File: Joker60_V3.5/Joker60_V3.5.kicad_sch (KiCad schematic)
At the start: 186 parts, among them J1 Conn_01x02, J2 Conn_01x04_MountingPin, J3 Conn_01x02, J4 Conn_01x02_MountingPin, J5 Conn_01x04_MountingPin, J6 Conn_01x06, U1 RP2040, U2 AMS1117-3.3, U3 W25Q128JVS, U4 2U卫星轴, U5 6.25u卫星轴, U6 2U卫星轴, U7 2U卫星轴, U8 2U卫星轴, U9 Oled_0.96_4P, Y1 Crystal

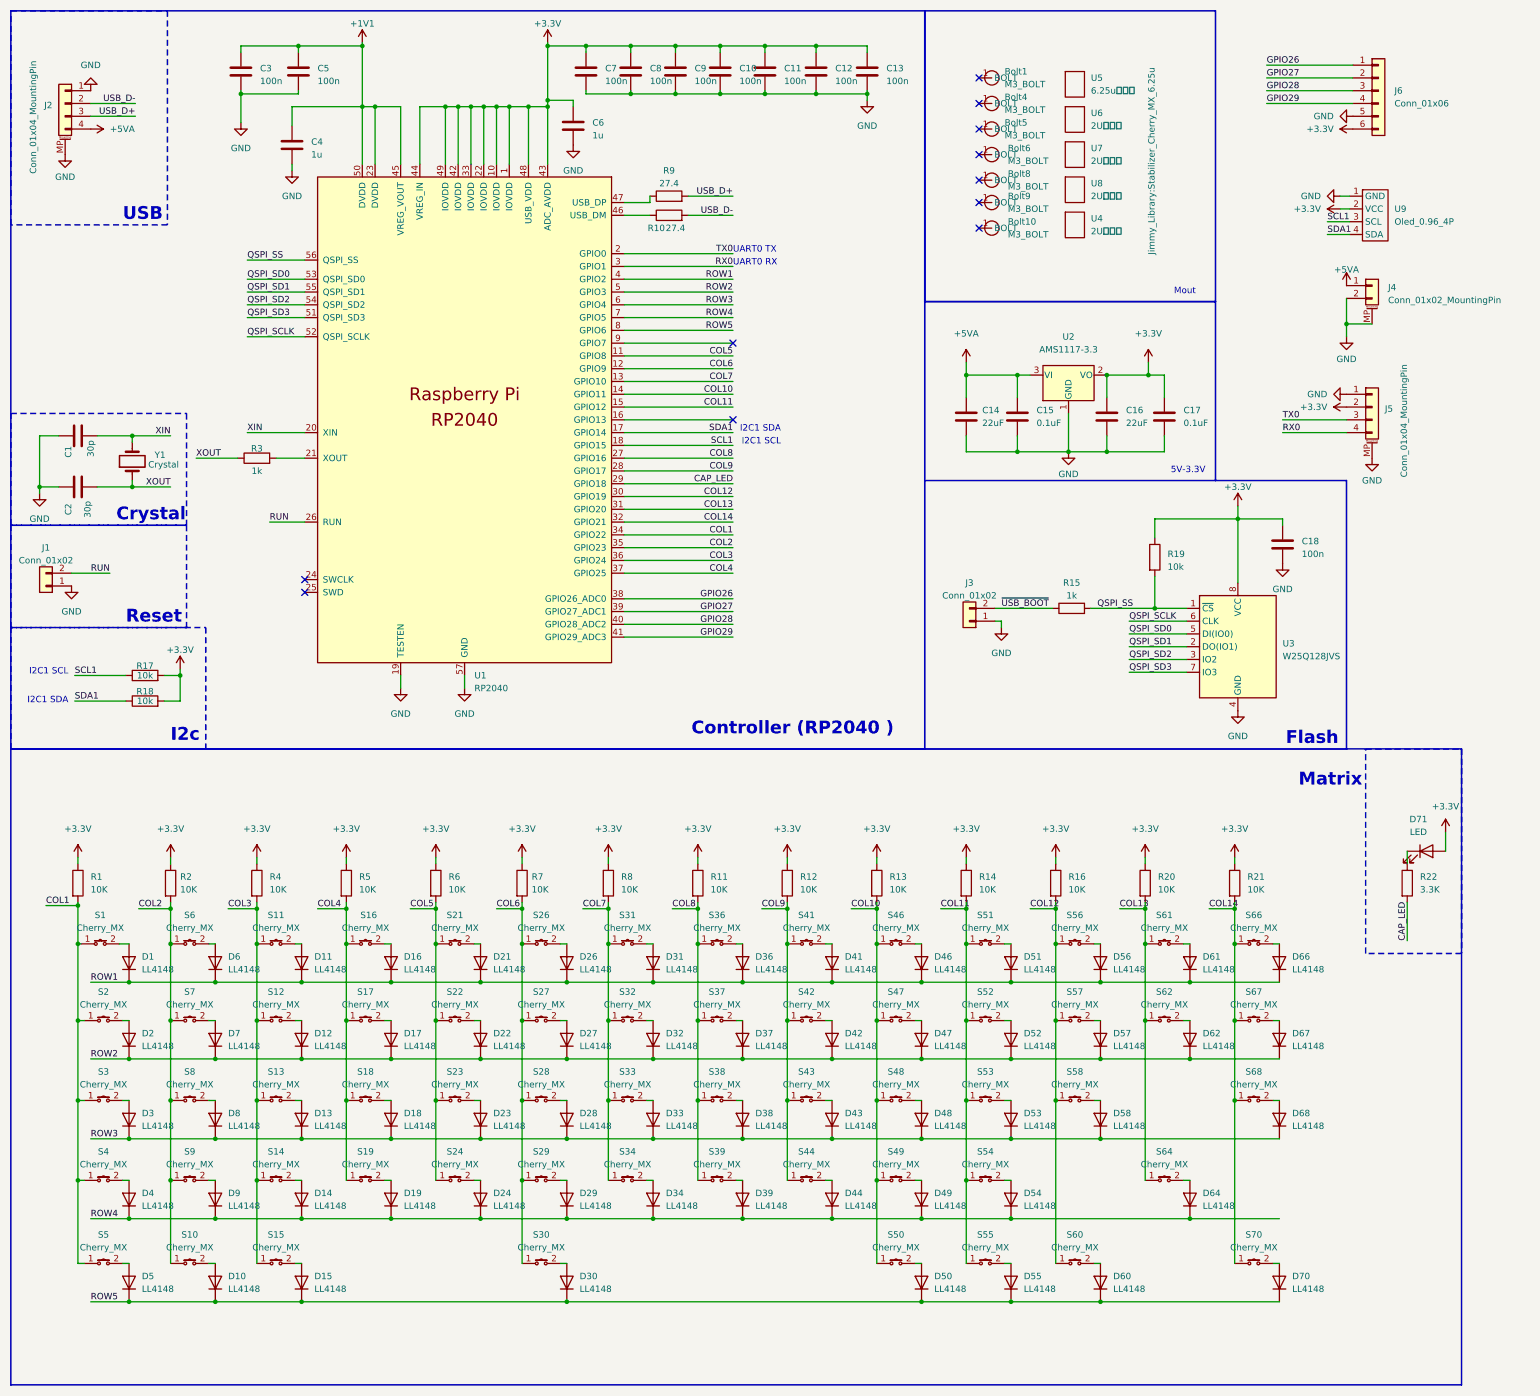
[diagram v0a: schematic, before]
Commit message: Start Building
Using Stm32f401, f103 should be compatible
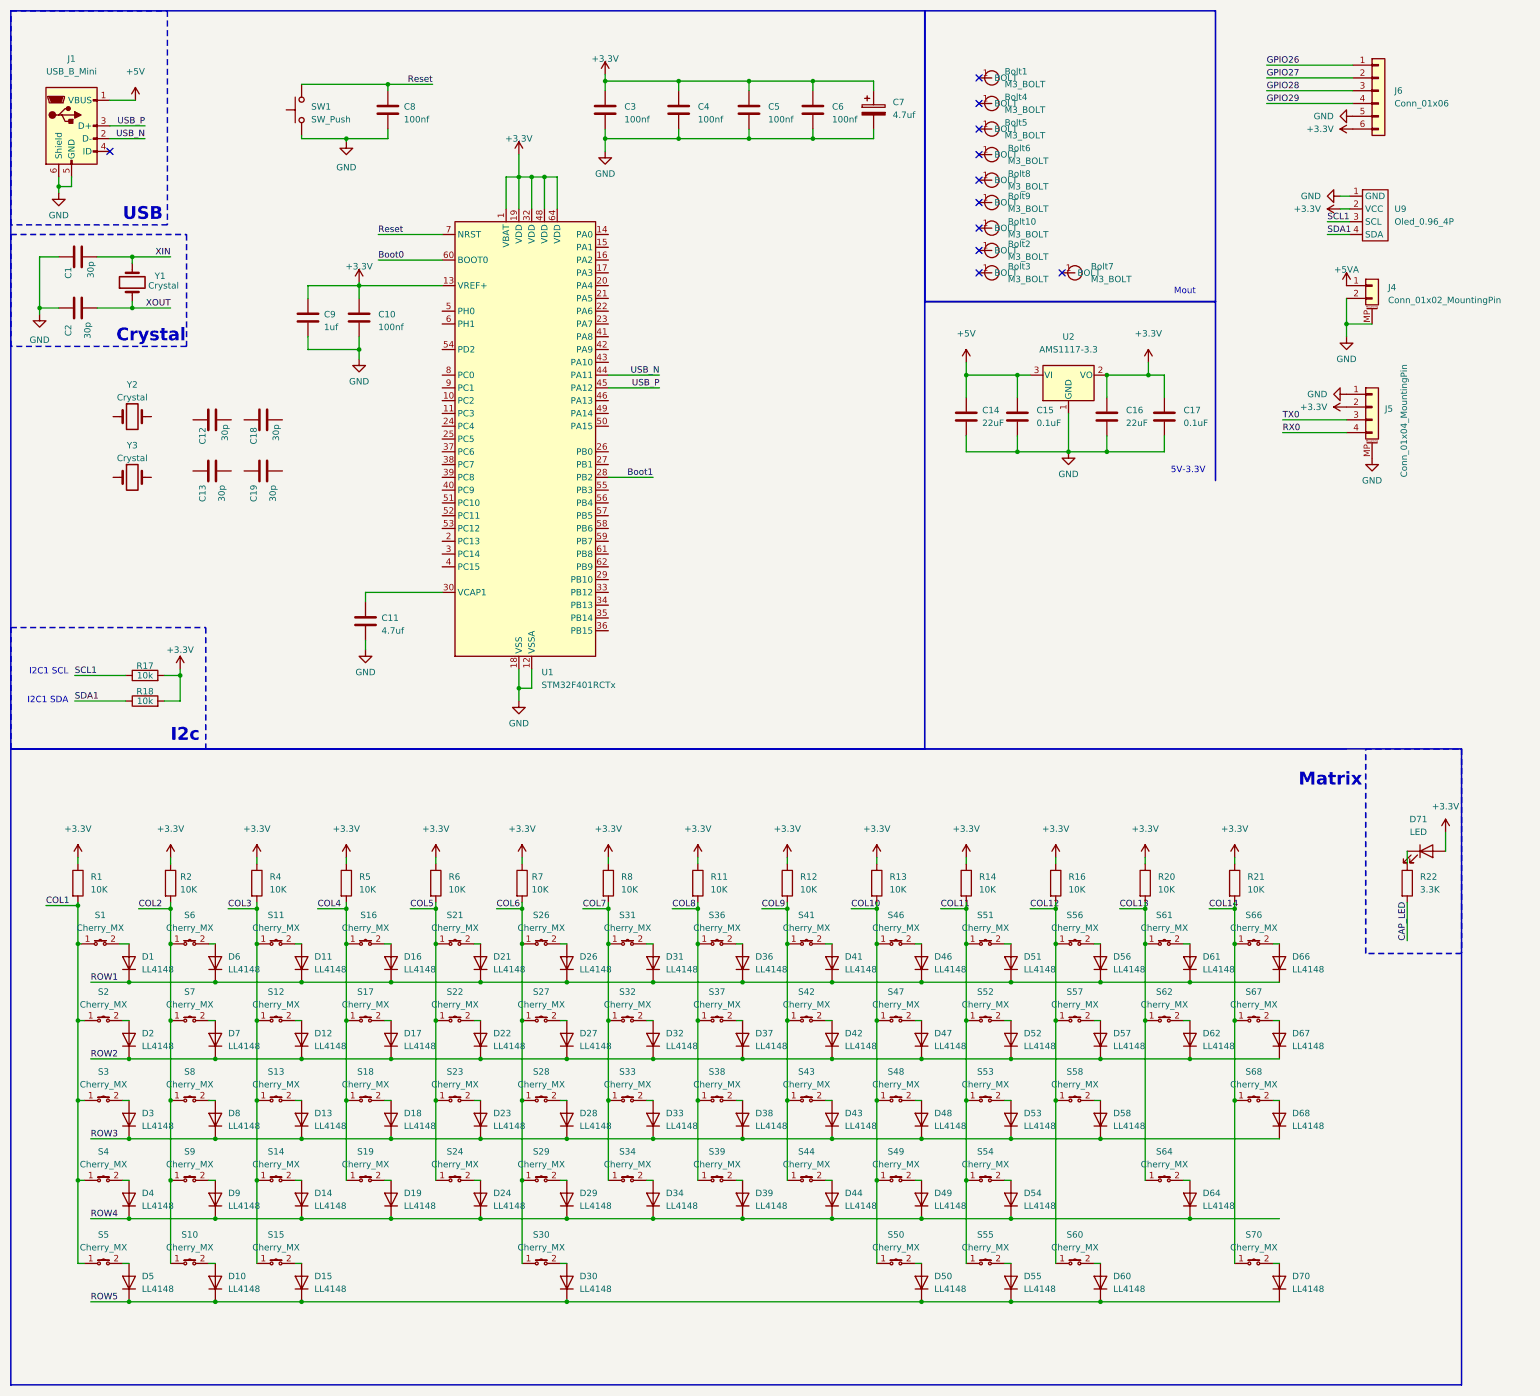
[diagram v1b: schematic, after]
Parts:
- removed C7: 100n, Capacitor_SMD:C_0402_1005Metric_Pad0.74x0.62mm_HandSolder, symbol Device:C
- removed J1, J3: Conn_01x02, Connector_PinHeader_2.54mm:PinHeader_1x02_P2.54mm_Vertical, symbol Connector_Generic:Conn_01x02
- removed J2: Conn_01x04_MountingPin, Connector_Molex:Molex_CLIK-Mate_502494-0470_1x04-1MP_P2.00mm_Horizontal, symbol Connector_Generic_MountingPin:Conn_01x04_MountingPin
- removed R10, R9: 27.4, Resistor_SMD:R_0402_1005Metric_Pad0.72x0.64mm_HandSolder, symbol Device:R
- removed R15: 1k, Resistor_SMD:R_0603_1608Metric_Pad0.98x0.95mm_HandSolder, symbol Device:R
- removed R19: 10k, Resistor_SMD:R_0603_1608Metric_Pad0.98x0.95mm_HandSolder, symbol Device:R
- removed R3: 1k, Resistor_SMD:R_0402_1005Metric_Pad0.72x0.64mm_HandSolder, symbol Device:R
- removed U1: RP2040, RP2040:QFN40P700X700X90-57N, symbol MCU_RaspberryPi_RP2040:RP2040
- removed U3: W25Q128JVS, Package_SO:SOIC-8_5.23x5.23mm_P1.27mm, symbol Memory_Flash:W25Q128JVS
- removed U4, U8: 2U卫星轴, Mounting_Keyboard_Stabilizer:Stabilizer_Cherry_MX_2.00u, symbol Jimmy_Library:2U卫星轴
- removed U5: 6.25u卫星轴, Jimmy_Library:Stabilizer_Cherry_MX_6.25u, symbol Jimmy_Library:6.25u卫星轴
- removed U6, U7: 2U卫星轴, Jimmy_Library:Stabilizer_Cherry_MX_2.00u, symbol Jimmy_Library:2U卫星轴
- added Bolt2, Bolt3, Bolt7: M3_BOLT, Jimmy_Library:M3 BOLT, symbol Jimmy_Library:M3_BOLT
- added C19: 30p, Capacitor_SMD:C_0603_1608Metric, symbol Device:C
- added C7: 4.7uf, Capacitor_Tantalum_SMD:CP_EIA-3216-18_Kemet-A, symbol Device:C_Polarized
- added J1: USB_B_Mini, Jimmy_Library:USB_Micro-B_4TH, symbol Connector:USB_B_Mini
- added SW1: SW_Push, symbol Switch:SW_Push
- added U1: STM32F401RCTx, Package_QFP:LQFP-64_10x10mm_P0.5mm, symbol MCU_ST_STM32F4:STM32F401RCTx
- added Y2, Y3: Crystal, Crystal:Crystal_SMD_3215-2Pin_3.2x1.5mm, symbol Device:Crystal
- C1, C2: footprint Capacitor_SMD:C_0402_1005Metric_Pad0.74x0.62mm_HandSolder -> Capacitor_SMD:C_0603_1608Metric
- C10, C3, C5, C8: value 100n -> 100nf; footprint Capacitor_SMD:C_0402_1005Metric_Pad0.74x0.62mm_HandSolder -> Capacitor_SMD:C_0603_1608Metric
- C11: value 100n -> 4.7uf; footprint Capacitor_SMD:C_0402_1005Metric_Pad0.74x0.62mm_HandSolder -> Capacitor_SMD:C_0603_1608Metric
- C12, C13: value 100n -> 30p; footprint Capacitor_SMD:C_0402_1005Metric_Pad0.74x0.62mm_HandSolder -> Capacitor_SMD:C_0603_1608Metric
- C14, C15, C16, C17: footprint Capacitor_SMD:C_0805_2012Metric_Pad1.18x1.45mm_HandSolder -> Capacitor_SMD:C_0603_1608Metric
- C18: value 100n -> 30p; footprint Capacitor_SMD:C_0603_1608Metric_Pad1.08x0.95mm_HandSolder -> Capacitor_SMD:C_0603_1608Metric
- C4, C6: value 1u -> 100nf; footprint Capacitor_SMD:C_0402_1005Metric_Pad0.74x0.62mm_HandSolder -> Capacitor_SMD:C_0603_1608Metric
- C9: value 100n -> 1uf; footprint Capacitor_SMD:C_0402_1005Metric_Pad0.74x0.62mm_HandSolder -> Capacitor_SMD:C_0603_1608Metric
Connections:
- net +1V1 is gone; now on net +3.3V: C3.1, C4.1, C5.1
- net +3.3V: now also C7.1, U1.1 (VBAT), U1.13 (VREF+), U1.19 (VDD), U1.32 (VDD), U1.48 (VDD), U1.64 (VDD); no longer C11.1, C12.1, C13.1, C18.1, C8.1
- net +5VA: no longer C14.1, C15.1, U2.3 (VI)
- net GND: now also C7.2, J1.5 (GND), J1.6 (Shield), SW1.1, U1.12 (VSSA), U1.18 (VSS), U1.31 (VSS), U1.47 (VSS), U1.63 (VSS); no longer C12.2, C13.2, C18.2
- new net: C11.1, U1.30 (VCAP1)
- new net +5V: C14.1, C15.1, J1.1 (VBUS), U2.3 (VI)
- new net Boot0: U1.60 (BOOT0)
- new net Boot1: U1.28 (PB2)
- new net Reset: C8.1, SW1.2, U1.7 (NRST)
- new net USB_N: J1.2 (D-), U1.44 (PA11)
- new net USB_P: J1.3 (D+), U1.45 (PA12)
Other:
- note removed: "Controller (RP2040 )"
- note removed: "Flash"
- note removed: "Reset"
- note removed: "UART0 RX"
- note removed: "UART0 TX"
- moved on the sheet: C1, C2, Y1

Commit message: 230814SchoolPC
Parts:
- removed C1, C13, C19, C2: 30p, Capacitor_SMD:C_0603_1608Metric, symbol Device:C
- removed D64: LL4148, Diode_SMD:D_MiniMELF, symbol Diode:LL4148
- removed S64: Cherry_MX, 0JIMMY:SW_Hotswap_Kailh_MX_plated_1.00u, symbol Cherry_MX:Cherry_MX
- removed SW1: SW_Push, symbol Switch:SW_Push
- removed Y1: Crystal, Crystal:Crystal_SMD_HC49-SD, symbol Device:Crystal
- removed Y3: Crystal, Crystal:Crystal_SMD_3215-2Pin_3.2x1.5mm, symbol Device:Crystal
- added D20: LL4148, Diode_SMD:D_MiniMELF, symbol Diode:LL4148
- added FB1: FerriteBead, Inductor_SMD:L_0805_2012Metric, symbol Device:FerriteBead
- added J2: Conn_01x02_Pin, Connector_PinHeader_2.54mm:PinHeader_1x02_P2.54mm_Vertical, symbol Connector:Conn_01x02_Pin
- added J3: Conn_02x07_Odd_Even, symbol Connector_Generic:Conn_02x07_Odd_Even
- added R3: 10k, Resistor_SMD:R_0805_2012Metric, symbol Device:R
- added S20: Cherry_MX, 0JIMMY:SW_Hotswap_Kailh_MX_plated_1.00u, symbol Cherry_MX:Cherry_MX
- Y2: value Crystal -> 25Mhz; footprint Crystal:Crystal_SMD_3215-2Pin_3.2x1.5mm -> Crystal:Crystal_SMD_5032-2Pin_5.0x3.2mm
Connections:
- net +3.3V: no longer C10.1, C16.1, C17.1, C3.1, C4.1, C5.1, C6.1, C7.1, C9.1, U1.1 (VBAT), U1.13 (VREF+), U1.19 (VDD), U1.32 (VDD), U1.48 (VDD), U1.64 (VDD), U2.2 (VO)
- net Boot0: now also R3.1
- net COL12: no longer S60.1
- net COL13: now also S60.1
- net COL14: now also S20.1
- net GND: now also C12.1, C18.1, J2.2 (Pin_2), R3.2
- net ROW4: now also D20.1 (K)
- net Reset: now also J2.1 (Pin_1)
- net RCC_OSC_IN: now reaches U1.5 (PH0)
- net RCC_OSC_IN: now also C12.2, Y2.1
- net RCC_OSC_OUT: now reaches U1.6 (PH1)
- net RCC_OSC_OUT: now also C18.2, Y2.2
- new net: D20.2 (A), S20.2
- new net VDD: C16.1, C17.1, C3.1, C4.1, C5.1, C6.1, C7.1, FB1.1, U1.1 (VBAT), U1.19 (VDD), U1.32 (VDD), U1.48 (VDD), U1.64 (VDD), U2.2 (VO)
- new net VDDA: C10.1, C9.1, FB1.2, U1.13 (VREF+)
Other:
- moved on the sheet: C10, C12, C18, C8, C9, D60, S60, Y2

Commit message: 230815_SchoolPC
PCB layout
CubeMX Pin configuration
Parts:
- removed J3: Conn_02x07_Odd_Even, symbol Connector_Generic:Conn_02x07_Odd_Even
- added H1, H2: MountingHole, MountingHole:MountingHole_2.2mm_M2_DIN965_Pad_TopBottom, symbol Mechanical:MountingHole
- added J3: Conn_02x10_Counter_Clockwise, J_Connecter:BTB_0.8mm_2x10pin_Female, symbol Connector_Generic:Conn_02x10_Counter_Clockwise
- added J7: Conn_01x04_Pin, Connector_PinHeader_2.54mm:PinHeader_1x04_P2.54mm_Vertical, symbol Connector:Conn_01x04_Pin
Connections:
- net +3.3V: no longer R1.1, R11.1, R12.1, R13.1, R14.1, R16.1, R2.1, R20.1, R21.1, R4.1, R5.1, R6.1, R7.1, R8.1
- net +5V: now also J3.1 (Pin_1), J3.2 (Pin_2)
- net COL10: now also U1.52 (PC11)
- net COL11: now also U1.53 (PC12)
- net COL12: now also U1.54 (PD2)
- net COL13: now also U1.55 (PB3)
- net COL14: now also U1.56 (PB4)
- net COL6: now also U1.58 (PB6)
- net COL7: now also U1.59 (PB7)
- net COL8: now also U1.61 (PB8)
- net COL9: now also U1.62 (PB9)
- net GND: now also J3.10 (Pin_10), J3.11 (Pin_11), J3.12 (Pin_12), J3.9 (Pin_9), J7.4 (Pin_4)
- net ROW1: now also U1.50 (PA15)
- net ROW2: now also U1.51 (PC10)
- net ROW3: now also U1.57 (PB5)
- net ROW4: now also U1.2 (PC13)
- net VDD: now also R1.1, R11.1, R12.1, R13.1, R14.1, R16.1, R2.1, R20.1, R21.1, R4.1, R5.1, R6.1, R7.1, R8.1, J3.19 (Pin_19), J3.20 (Pin_20), J7.1 (Pin_1)
- net PB12: now reaches U1.33 (PB12)
- net PB12: now also J3.18 (Pin_18)
- net SCK2: now reaches U1.34 (PB13)
- net SCK2: now also J3.17 (Pin_17)
- net MISO2: now reaches U1.35 (PB14)
- net MISO2: now also J3.16 (Pin_16)
- net MOSI2: now reaches U1.36 (PB15)
- net MOSI2: now also J3.15 (Pin_15)
- net Tx6: now reaches U1.37 (PC6)
- net Tx6: now also J3.3 (Pin_3)
- net Rx6: now reaches U1.38 (PC7)
- net Rx6: now also J3.4 (Pin_4)
- net SDA3: now reaches U1.40 (PC9)
- net SDA3: now also J3.7 (Pin_7)
- net SCL3: now reaches U1.41 (PA8)
- net SCL3: now also J3.8 (Pin_8)
- net SWDIO: now reaches U1.46 (PA13)
- net SWDIO: now also J7.2 (Pin_2)
- net SWDCLK: now reaches U1.49 (PA14)
- net SWDCLK: now also J7.3 (Pin_3)

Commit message: 230816_SchoolPC
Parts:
- removed D71: LED, LED_SMD:LED_0805_2012Metric_Pad1.15x1.40mm_HandSolder, symbol Device:LED
- removed J4: Conn_01x02_MountingPin, Connector_Molex:Molex_CLIK-Mate_502494-0270_1x02-1MP_P2.00mm_Horizontal, symbol Connector_Generic_MountingPin:Conn_01x02_MountingPin
- removed J5: Conn_01x04_MountingPin, Connector_Molex:Molex_CLIK-Mate_502494-0470_1x04-1MP_P2.00mm_Horizontal, symbol Connector_Generic_MountingPin:Conn_01x04_MountingPin
- removed J6: Conn_01x06, Connector_Molex:Molex_CLIK-Mate_502443-0670_1x06-1MP_P2.00mm_Vertical, symbol Connector_Generic:Conn_01x06
- removed U9: Oled_0.96_4P, Connector_Molex:Molex_CLIK-Mate_502494-0470_1x04-1MP_P2.00mm_Horizontal, symbol Jimmy_Library:Oled_0.96_4P
- added D25, D35: LED, LED_SMD:LED_1206_3216Metric_Pad1.42x1.75mm_HandSolder, symbol Device:LED
- added R9: 3.3K, Resistor_SMD:R_0603_1608Metric_Pad0.98x0.95mm_HandSolder, symbol Device:R
- added TP1: TestPoint, TestPoint:TestPoint_Pad_1.5x1.5mm, symbol Connector:TestPoint
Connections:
- net +3.3V is gone; now on net VDD: R17.2, R18.2
- net CAP_LED is gone; now on net LED2: R22.2
- net SCL1 is gone; now on net SCL3: R17.1
- net SDA1 is gone; now on net SDA3: R18.1
- net Boot1: now also TP1.1
- net COL1: now also U1.17 (PA3)
- net COL2: now also U1.20 (PA4)
- net COL3: now also U1.21 (PA5)
- net COL4: now also U1.16 (PA2)
- net COL5: now also U1.15 (PA1)
- net GND: now also J3.13 (Pin_13), J3.5 (Pin_5), J3.6 (Pin_6)
- net ROW5: now also U1.14 (PA0)
- net VDD: now also D25.2 (A), D35.2 (A)
- net at R22.1: now also D25.1 (K)
- net LED1: now reaches U1.22 (PA6)
- net LED1: now also R9.2
- net LED2: now reaches U1.23 (PA7)
- net PC8: now reaches U1.39 (PC8)
- net PC8: now also J3.14 (Pin_14)
- new net: D35.1 (K), R9.1
- no-connect marks 11 -> 19

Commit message: 230817_schoolPC
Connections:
- no-connect marks 19 -> 24
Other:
- company: (none) -> Liu Zeshu
- title: (none) -> Joker 60 v3.5
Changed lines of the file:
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@@
 (kicad_sch (version 20230121) (generator eeschema)
   (paper "A3")
+  (title_block
+    (title "Joker 60 v3.5")
+    (date "2023-08-17")
+    (rev "Rev 1.0")
+    (company "Liu Zeshu")
+  )
   (junction (at 184.15 244.475) (diameter 0) (color 0 0 0 0)
   )
@@
   (junction (at 193.04 220.345) (diameter 0) (color 0 0 0 0)
   )
+  (no_connect (at 97.79 94.615))
+  (no_connect (at 130.81 102.235))
+  (no_connect (at 130.81 99.695))
   (no_connect (at 204.47 50.165))
   (no_connect (at 204.47 30.48))
@@
   (no_connect (at 204.47 59.69))
   (no_connect (at 204.47 45.72))
+  (no_connect (at 97.79 97.155))
   (no_connect (at 204.47 55.245))
+  (no_connect (at 130.81 125.095))
   (wire (pts (xy 87.63 236.22) (xy 105.41 236.22))
     (stroke (width 0) (type default))
@@
     (stroke (width 0) (type default))
   )
+  (polyline (pts (xy 193.675 105.41) (xy 251.46 105.41))
+    (stroke (width 0.3) (type default))
+  )
   (wire (pts (xy 122.555 260.985) (xy 121.285 260.985))
     (stroke (width 0) (type default))
@@
     )
   )
-  (symbol (lib_id "power:GND") (at 82.55 139.065 0) (unit 1)
+  (symbol (lib_name "GND_2") (lib_id "power:GND") (at 82.55 139.065 0) (unit 1)
     (in_bom yes) (on_board yes) (dnp no) (fields_autoplaced)
     (property "Reference" "#PWR016" (at 82.55 145.415 0)
